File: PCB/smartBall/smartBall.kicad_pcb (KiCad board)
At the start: 2 copper layers, 116 parts, among them IC1 NEO-F10N-00B, IC10 BQ51013BRHLR, IC11 TPS61032PWP, IC12 ADM7155ACPZ-04-R7, IC13 TXB0108PWR, IC3 ESP32-S3-WROOM-1-N4R8, IC4 TPS63000IDRCRQ1, IC5 MAX17048G+T10, IC6 4259-63, IC7 ADM7155ACPZ-04-R7, IC8 MAX98357AETE+T, IC9 LSM6DSV16BXTR, J1 UJ20-C-H-G-MSMT-R-4C-P16-TR, J10 Conn_01x15, J2 Speaker, J3 QVAR, J4 FXP612 (u.FL) 2, J5 FXP612 (u.FL) 1, J6 SIM8055-6-1-14-00-A, J7 FXP612 (u.FL) 1, J8 Conn_01x02, J9 Conn_01x15, Q2 BSS138, Q3 Si2323DDS-T1-GE3, Q4 BSS138, Q5 BSS138, Q6 Si2323DDS-T1-GE3, U1 MCP73871-2CA, U2 SIM7000G

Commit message: pcb start
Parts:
- moved U1 195.9 mm to (236.1, 140.0)
- moved BT1 181.8 mm to (221.2, 149.5)
- moved IC10 176.3 mm to (205.8, 141.4)
- moved J1 174.1 mm to (231.9, 88.9)
- moved D3 172.4 mm to (236.2, 80.5)
- moved IC12 168.9 mm to (207.6, 126.8)
- moved IC5 160.9 mm to (216.0, 134.8)
- moved IC3 156.4 mm to (195.5, 43.5), turned to 180 degrees
- moved J2 151.9 mm to (235.5, 36.5)
- moved TP2 138.5 mm to (239.5, 50.0)
- moved J6 134.3 mm to (214.5, 33.3), turned to 180 degrees
- moved TP4 132.4 mm to (232.5, 29.5)
- moved U2 132.1 mm to (222.5, 55.5), turned to 180 degrees
- moved TP5 131.7 mm to (237.0, 29.5)
- moved TP1 131.3 mm to (228.5, 29.5)
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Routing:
- net IMU_CS: track 0.00 -> 65.2 mm
- net WCLK: track 0.00 -> 60.1 mm
- net IMU_INT1: track 0.00 -> 49.1 mm, vias 0 -> 2
- net BCLK: track 0.00 -> 48.1 mm
- net MISO: track 0.00 -> 44.3 mm
- net SCLK: track 0.00 -> 38.6 mm, vias 0 -> 2
- net MOSI: track 0.00 -> 38.0 mm
- net DATA_IN: track 0.00 -> 36.9 mm, vias 0 -> 2
- net ACCEL_CS: track 0.00 -> 30.3 mm
- net ACCEL_INT1: track 0.00 -> 25.2 mm
- net GND: track 0.00 -> 24.4 mm, vias 0 -> 2
- net Net-(U2-MDM_LOG_TX): track 0.00 -> 8.40 mm
- net Net-(U2-USB_DM): track 0.00 -> 6.54 mm
- net Net-(U2-USB_VBUS): track 0.00 -> 6.12 mm
- net Net-(U2-USB_DP): track 0.00 -> 5.71 mm
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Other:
- board outline added: 134 x 174.5 mm

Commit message: updated to hierarchical labels
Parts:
- J6, TP1, TP2, TP3, TP4, TP5, TP6, U2: moved to B.Cu
- moved R29 130.1 mm to (172.7, 38.0)
- moved Q2 107.7 mm to (226.3, 51.5)
- moved D6 49.3 mm to (23.9, 107.0)
- moved C22 47.6 mm to (154.5, 22.5)
- moved C12 34.3 mm to (148.2, 29.0)
- moved R10 32.9 mm to (34.7, 140.0)
- moved C26 32.9 mm to (143.5, 22.0)
- moved S2 23.0 mm to (196.6, 90.5)
- moved C24 22.6 mm to (120.8, 24.5)
- moved C13 19.5 mm to (131.5, 24.0)
- moved C25 15.3 mm to (106.3, 34.0)
- moved J7 11.2 mm to (123.0, 42.0)
- moved IC3 11.0 mm to (206.5, 44.0), turned to 0 degrees
- moved C23 9.72 mm to (111.8, 27.5)
- moved R22 8.66 mm to (69.0, 95.2), turned to -90 degrees
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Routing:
- net IMU_CS: track 65.2 -> 0.00 mm
- net WCLK: track 60.1 -> 0.00 mm
- net IMU_INT1: track 49.1 -> 0.00 mm, vias 2 -> 0
- net BCLK: track 48.1 -> 0.00 mm
- net MISO: track 44.3 -> 0.00 mm
- net SCLK: track 38.6 -> 0.00 mm, vias 2 -> 0
- net MOSI: track 38.0 -> 0.00 mm
- net DATA_IN: track 36.9 -> 0.95 mm, vias 2 -> 0
- net ACCEL_CS: track 30.3 -> 0.00 mm
- net ACCEL_INT1: track 25.2 -> 0.53 mm
- net GND: track 24.4 -> 0.00 mm, vias 2 -> 0
- net Net-(U2-MDM_LOG_TX): track 8.40 -> 0.00 mm
- net Net-(U2-USB_DM): track 6.54 -> 0.00 mm
- net Net-(U2-USB_VBUS): track 6.12 -> 0.00 mm
- net Net-(U2-USB_DP): track 5.71 -> 0.71 mm
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
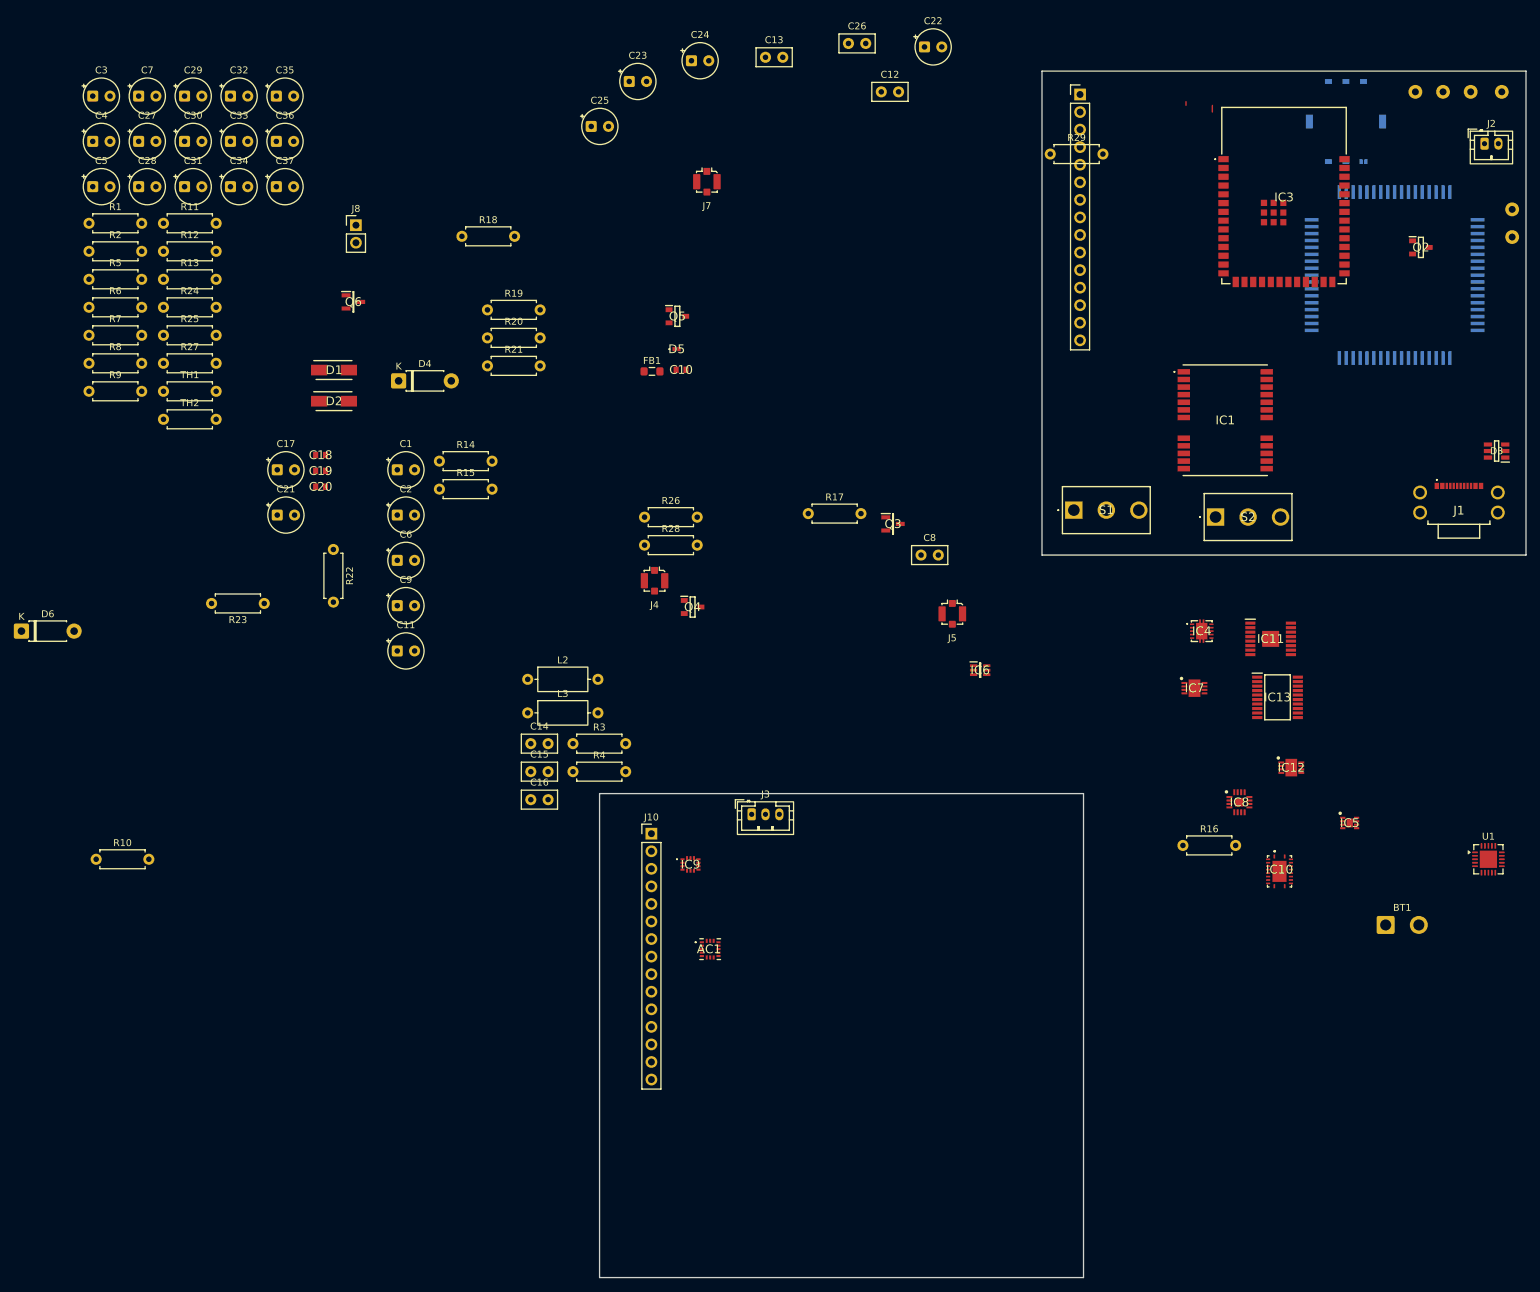
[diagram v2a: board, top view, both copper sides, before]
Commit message: new footprints assigned
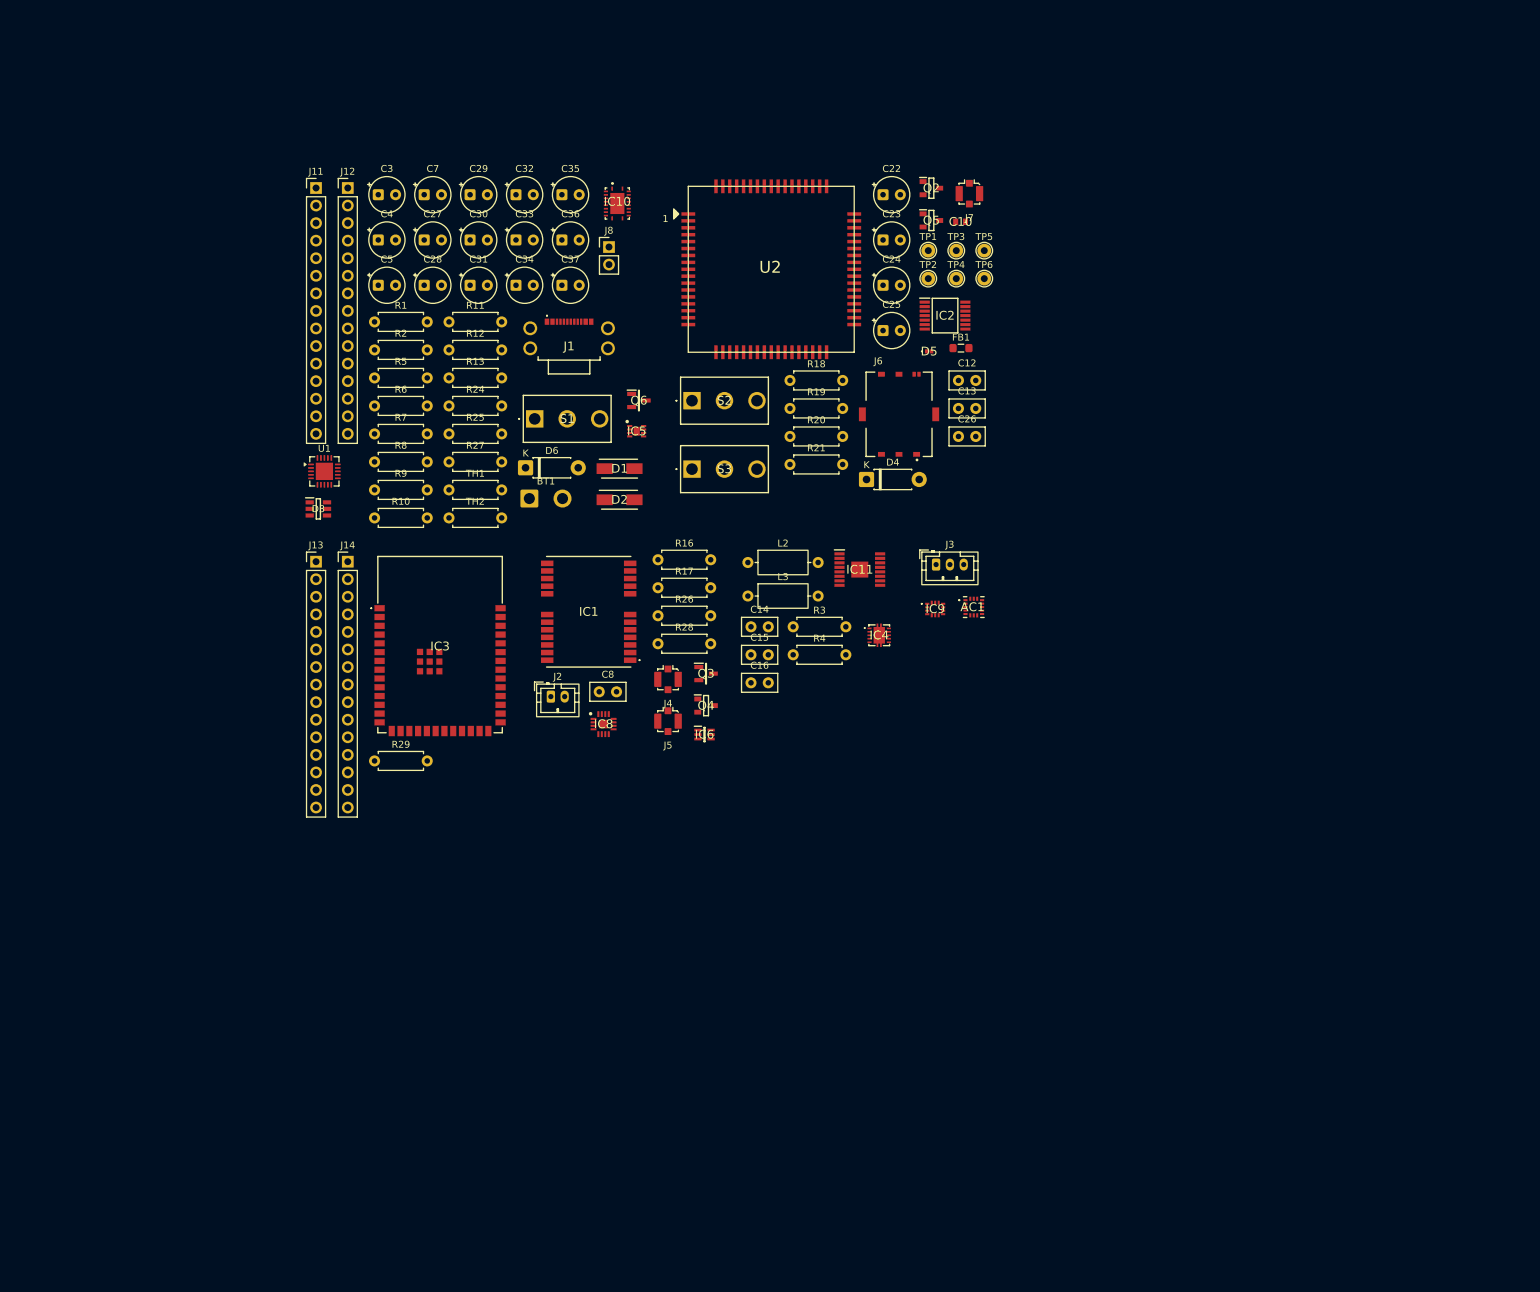
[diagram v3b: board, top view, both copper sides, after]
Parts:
- removed C1, C9: 1µF, Capacitor_THT:CP_Radial_Tantal_D5.0mm_P2.50mm
- removed C11, C17, C2, C21, C6: 10µF, Capacitor_THT:CP_Radial_Tantal_D5.0mm_P2.50mm
- removed C18, C19, C20: CL10B105KO8NNNC, CL10B105KO8NNNC:CAPC1608X90N
- removed IC12, IC7: ADM7155ACPZ-04-R7, ADM7155ACPZ-04-07:SON50P300X300X80-9N-D
- removed IC13: TXB0108PWR, TXB0108PWR:SOP65P640X120-20N
- removed J10, J9: Conn_01x15, Connector_PinHeader_2.54mm:PinHeader_1x15_P2.54mm_Vertical
- removed R14: 175kΩ, Resistor_THT:R_Axial_DIN0207_L6.3mm_D2.5mm_P7.62mm_Horizontal
- removed R15: 100kΩ, Resistor_THT:R_Axial_DIN0207_L6.3mm_D2.5mm_P7.62mm_Horizontal
- removed R22: 17.5kΩ, Resistor_THT:R_Axial_DIN0207_L6.3mm_D2.5mm_P7.62mm_Horizontal
- removed R23: 10kΩ, Resistor_THT:R_Axial_DIN0207_L6.3mm_D2.5mm_P7.62mm_Horizontal
- added IC2: TXB0104PWR, Smartball_footprints:SOP65P640X120-14N, F.Cu at (157.5, 61.4)
- added J11: Conn_01x15, Connector_PinHeader_2.54mm:PinHeader_1x15_P2.54mm_Vertical, F.Cu at (66.5, 42.9)
- added J12: Conn_01x15, Connector_PinHeader_2.54mm:PinHeader_1x15_P2.54mm_Vertical, F.Cu at (71.1, 42.9)
- added J13: Conn_01x15, Connector_PinHeader_2.54mm:PinHeader_1x15_P2.54mm_Vertical, F.Cu at (66.5, 97.0)
- added J14: Conn_01x15, Connector_PinHeader_2.54mm:PinHeader_1x15_P2.54mm_Vertical, F.Cu at (71.1, 97.0)
- added S3: SLW-1276864-4A-D, SLW-1276864-4A-D:SLW12768644AD, F.Cu at (120.9, 83.6)
- D5: footprint PESD3V3L1BSL:PESD3V3L1BSLZ -> PESD3V3L1BSLZ:PESD3V3L1BSLZ
- IC3: footprint ESP_32-S3-WROOM-1-N4R8:ESP32S3WROOM1N4R8 -> ESP32-S3-WROOM-1-N4R8/:ESP32S3WROOM1N4R8
- IC4: footprint TPS63000DRCRQ1:TPS63000IDRCRQ1 -> TPS63000IDRCRQ1:TPS63000IDRCRQ1
- J6, TP1, TP2, TP3, TP4, TP5, TP6, U2: moved to F.Cu
- moved U1 177.5 mm to (67.7, 83.9)
- moved D3 170.6 mm to (66.8, 89.3), turned to 0 degrees
- moved J2 156.9 mm to (100.5, 116.5)
- moved BT1 138.4 mm to (97.3, 87.8)
- moved IC3 138.3 mm to (84.4, 109.0)
- moved IC10 136.0 mm to (110.1, 44.8)
- moved R29 131.4 mm to (75.0, 125.8)
- moved J1 130.9 mm to (103.1, 66.0)
- moved IC5 117.7 mm to (112.9, 78.1)
- moved IC1 96.1 mm to (105.9, 104.2), turned to 0 degrees
- moved IC8 92.7 mm to (108.1, 120.5)
- moved U2 90.2 mm to (132.3, 54.7)
- moved R16 86.4 mm to (116.0, 96.7)
- moved TP2 84.7 mm to (155.0, 56.0), turned to 0 degrees
- moved TP4 79.2 mm to (159.1, 56.0), turned to 0 degrees
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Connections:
- net +5V renamed /OUT+5V
- net ANTENA_SW renamed /ANTENA_SW
- net GPS_INT renamed /GSM_INT
- net GPS_POWER renamed /GSM_POWER
- net OUT+5V renamed /Power/STEP_UP/OUT+5V
- net TIMEPULSE renamed /TIMEPULSE
- net V_SYS renamed /Power/V_SYS
- AC1 pad 1: VOUT_3V3 -> /Power/Movement/VOUT_3V3
- AC1 pad 11: ACCEL_INT1 -> /Power/Movement/ACCEL_INT1
- AC1 pad 14: VOUT_3V3 -> /Power/Movement/VOUT_3V3
- AC1 pad 4: SCLK -> /Power/Movement/SCLK
- AC1 pad 6: MOSI -> /Power/Movement/MOSI
- AC1 pad 7: MISO -> /Power/Movement/MISO
- AC1 pad 8: ACCEL_CS -> /Power/Movement/ACCEL_CS
- AC1 pad 9: ACCEL_INT2 -> /Power/Movement/ACCEL_INT2
- BT1 pad 1: BAT+ -> /Power/BAT+
- C27 pad 2: BAT+ -> /Power/BAT+
- C29 pad 1: BAT+ -> /Power/BAT+
- C8 pad 1: VOUT_3V3 -> Net-(IC1-V_BCKP)
- D3 pad 1: USB_D+ -> /Power/USB_D+
- D3 pad 3: USB_D- -> /Power/USB_D-
- D3 pad 4: USB_D- -> /Power/USB_D-
- D3 pad 6: USB_D+ -> /Power/USB_D+
- IC1 pad 20: TXD -> /TXD
- IC1 pad 21: RXD -> /RXD
- IC1 pad 22: VOUT_3V3 -> Net-(IC1-V_BCKP)
- IC11 pad 9: LOUDNESS -> /Power/STEP_UP/LOUDNESS
- IC3 pad 10: MOSI -> /MISO
- IC3 pad 11: SCLK -> /MOSI
- IC3 pad 12: MISO -> /SCLK
- IC3 pad 13: LOUDNESS -> /LOUDNESS
- IC3 pad 14: G_BCLK -> /G_LRCLK
- IC3 pad 15: G_LRCLK -> G_DIN
- IC3 pad 16: G_DIN -> /G_BCLK
- IC3 pad 17: IMU_CS -> /IMU_CS
- IC3 pad 18: WCLK -> /WCLK
- IC3 pad 19: BCLK -> /BCLK
- IC3 pad 2: /V_ESP -> /+3V3
- IC3 pad 20: DATA_IN -> /DATA_IN
- IC3 pad 21: IMU_INT1 -> /IMU_INT1
- IC3 pad 22: ACCEL_CS -> /ACCEL_CS
- IC3 pad 23: ACCEL_INT1 -> /ACCEL_INT1
- IC3 pad 24: FG_ALRT -> /FG_ALTR
- IC3 pad 25: STAT1 -> /STAT1
- IC3 pad 26: GSM_RXD -> /GSM_RXT
- IC3 pad 27: GSM_TXD -> /GSM_TXD
- IC3 pad 28: GSM_STATUS -> unconnected-(IC3-IO35-Pad28)
- IC3 pad 29: GSM_CTS -> unconnected-(IC3-IO36-Pad29)
- IC3 pad 30: GSM_DCD -> unconnected-(IC3-IO37-Pad30)
- IC3 pad 31: GSM_RI -> unconnected-(IC3-IO38-Pad31)
- IC3 pad 32: GSM_DCD -> unconnected-(IC3-IO39-Pad32)
- IC3 pad 33: GSM_DTR -> unconnected-(IC3-IO40-Pad33)
- IC3 pad 34: STAT2 -> /STA2
- IC3 pad 36: I2C_SCL -> /I2C_SCL
- IC3 pad 37: I2C_SDA -> /I2C_SDA
- IC3 pad 38: USB_D- -> /USB_D-
- IC3 pad 39: USB_D+ -> /USB_D+
- IC3 pad 4: RXD -> /GSM_TXD
- IC3 pad 5: TXD -> /GSM_RXT
- IC4 pad 1: +3V3 -> /Power/Movement/VOUT_3V3
- IC5 pad 2: BAT+ -> /Power/BAT+
- IC5 pad 3: BAT+ -> /Power/BAT+
- IC5 pad 5: FG_ALRT -> /Power/FG_ALRT
- IC5 pad 7: I2C_SCL -> /Power/I2C_SCL
- IC5 pad 8: I2C_SDA -> /Power/I2C_SDA
- IC8 pad 14: G_LRCLK -> /G_LRCLK
- IC8 pad 16: G_BCLK -> /G_BCLK
- IC9 pad 1: MISO -> /Power/Movement/MISO
- IC9 pad 10: IMU_INT2 -> /Power/Movement/IMU_INT2
- IC9 pad 11: WCLK -> unconnected-(IC9-WCLK-Pad11)
- IC9 pad 12: IMU_CS -> /Power/Movement/IMU_CS
- IC9 pad 13: SCLK -> /Power/Movement/SCLK
- IC9 pad 14: MOSI -> /Power/Movement/MOSI
- IC9 pad 2: DATA_IN -> /Power/Movement/DATA_IN
- IC9 pad 3: BCLK -> /Power/Movement/BCLK
- IC9 pad 4: IMU_INT1 -> /Power/Movement/IMU_INT1
- IC9 pad 5: VOUT_3V3 -> /Power/Movement/VOUT_3V3
- IC9 pad 8: VOUT_3V3 -> /Power/Movement/VOUT_3V3
- J1 pad A6: USB_D+ -> /Power/USB_D+
- J1 pad A7: USB_D- -> /Power/USB_D-
- J1 pad B6: USB_D+ -> /Power/USB_D+
- J1 pad B7: USB_D- -> /Power/USB_D-
- Q3 pad 2: VOUT_3V3 -> /+3V3
- Q4 pad 1: LOUDNESS -> /LOUDNESS
- R18 pad 2: VOUT_3V3 -> /+3V3
- R24 pad 1: STAT1 -> /Power/STAT1
- R25 pad 1: STAT2 -> /Power/STAT2
- R29 pad 2: /V_ESP -> /+3V3
- R3 pad 2: +3V3 -> /Power/Movement/VOUT_3V3
- R5 pad 1: +3V3 -> /Power/Movement/VOUT_3V3
- R5 pad 2: I2C_SDA -> /Power/I2C_SDA
- R6 pad 1: +3V3 -> /Power/Movement/VOUT_3V3
- R6 pad 2: I2C_SCL -> /Power/I2C_SCL
- R7 pad 1: +3V3 -> /Power/Movement/VOUT_3V3
- R7 pad 2: FG_ALRT -> /Power/FG_ALRT
- S2 pad 2: BAT+ -> Net-(S2-COM)
- U1 pad 14: BAT+ -> /Power/BAT+
- U1 pad 15: BAT+ -> /Power/BAT+
- U1 pad 16: BAT+ -> /Power/BAT+
- U1 pad 7: STAT2 -> /Power/STAT2
- U1 pad 8: STAT1 -> /Power/STAT1
- U2 pad P$10: GSM_RXD -> /GSM_RXT
- U2 pad P$3: /Stationary/GSM_sheet/DTR -> unconnected-(U2-DTR-PadP$3)
- U2 pad P$4: /Stationary/GSM_sheet/RI -> unconnected-(U2-RI-PadP$4)
- U2 pad P$5: /Stationary/GSM_sheet/DCD -> unconnected-(U2-DCD-PadP$5)
- U2 pad P$7: GSM_CTS -> unconnected-(U2-CTS-PadP$7)
- U2 pad P$8: GSM_RTS -> unconnected-(U2-RTS-PadP$8)
- U2 pad P$9: GSM_TXD -> /GSM_TXD
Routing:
- net DATA_IN: track 0.95 -> 0.00 mm
- net Net-(U2-USB_DP): track 0.71 -> 0.00 mm
- net ACCEL_INT1: track 0.53 -> 0.00 mm
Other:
- board outline removed

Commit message: last modifications schematic
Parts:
- moved J13 210.2 mm to (263.2, 23.0), turned to -90 degrees
- moved J14 204.7 mm to (266.0, 34.4)
- moved IC3 175.4 mm to (248.8, 47.7), turned to 180 degrees
- moved R29 169.8 mm to (225.0, 46.2), turned to -90 degrees
- moved J2 165.4 mm to (263.0, 86.0)
- moved IC8 161.1 mm to (264.0, 80.0)
- moved IC10 147.9 mm to (67.8, 186.5)
- moved IC1 129.7 mm to (213.0, 31.0)
- moved J1 129.5 mm to (133.4, 191.9)
- moved J12 128.0 mm to (160.0, 135.0), turned to -90 degrees
- moved R8 113.4 mm to (119.0, 187.0), turned to -90 degrees
- moved D3 112.9 mm to (132.8, 181.0)
- moved U1 110.1 mm to (111.5, 184.9)
- moved J11 100.0 mm to (103.0, 136.0)
- moved J6 94.9 mm to (245.7, 78.0)
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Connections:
- net G_DIN renamed /G_DIN
- C8 pad 1: Net-(IC1-V_BCKP) -> /+3V3
- IC1 pad 20: /TXD -> /RXD
- IC1 pad 21: /RXD -> /TXD
- IC1 pad 22: Net-(IC1-V_BCKP) -> /+3V3
- IC10 pad 13: Net-(IC10-TS/CTRL) -> /Power/TS/CTRL
- IC2 pad 10: unconnected-(IC2-B4-Pad10) -> /STATUS
- IC2 pad 11: unconnected-(IC2-B3-Pad11) -> /PWRKEY
- IC2 pad 4: unconnected-(IC2-A3-Pad4) -> /PWRKEY
- IC2 pad 5: unconnected-(IC2-A4-Pad5) -> /STATUS
- IC3 pad 28: unconnected-(IC3-IO35-Pad28) -> /ACCEL_INT2
- IC3 pad 29: unconnected-(IC3-IO36-Pad29) -> /IMU_INT2
- IC3 pad 30: unconnected-(IC3-IO37-Pad30) -> /TS/CTRL
- IC3 pad 31: unconnected-(IC3-IO38-Pad31) -> /PWRKEY
- IC3 pad 32: unconnected-(IC3-IO39-Pad32) -> /STATUS
- IC3 pad 34: /STA2 -> /STAT2
- IC3 pad 35: PWRKEY -> unconnected-(IC3-IO42-Pad35)
- IC3 pad 4: /GSM_TXD -> /TXD
- IC3 pad 5: /GSM_RXT -> /RXD
- IC5 pad 9: unconnected-(IC5-EP-Pad9) -> GND
- IC9 pad 11: unconnected-(IC9-WCLK-Pad11) -> /Power/Movement/WCLK
- J11 pad 2: unconnected-(J11-Pin_2-Pad2) -> /Power/TS/CTRL
- J13 pad 4: /BLCK -> /BCLK
- J14 pad 2: unconnected-(J14-Pin_2-Pad2) -> /TS/CTRL
- J14 pad 9: /FG_ALRT -> /FG_ALTR
- S3 pad 3: unconnected-(S3-NO-Pad3) -> /OUT+5V
- TH2 pad 1: unconnected-(TH2-Pad1) -> GND
- TH2 pad 2: Net-(IC10-TS/CTRL) -> /Power/TS/CTRL
- U2 pad P$1: Net-(Q2-D) -> /PWRKEY
- U2 pad P$66: /Stationary/GSM_sheet/STATUS -> /STATUS
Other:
- board outline added: 172 x 179 mm

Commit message: everything before jlc template
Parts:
- moved J1 62.5 mm to (113.0, 251.0)
- moved D3 58.5 mm to (146.2, 237.9)
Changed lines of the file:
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@@
 	(footprint "UJ20-C-H-G-MSMT-R-4C-P16-TR:UJ20CHGMSMTR4CP16TR"
 		(layer "F.Cu")
-		(at 133.38 191.925)
+		(at 113 251)
 		(descr "UJ20-C-H-G-MSMT-R-4C-P16-TR-3")
 		(tags "Connector")
@@
 	(footprint "USBLC6-2SC6Y:SOT95P280X145-6N"
 		(layer "F.Cu")
-		(at 132.75 181)
+		(at 146.25 237.95)
 		(descr "<b>SOT23-6(ESDA6V1-5SC6Y)</b><br>")
 		(property "Reference" "D3"
